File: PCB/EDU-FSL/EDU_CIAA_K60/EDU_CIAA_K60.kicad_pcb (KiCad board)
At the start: 2 copper layers, 137 x 86 mm, 188 parts, among them J1 USB OTG, J2 TB_1X2, J3 JTAG DEBUG USB, J4 JTAG DIRECTO, J5 RS485, P1 CONN_20X2, P2 CONN_20X2, Q1 2N7002, Q2 2N7002, Q3 2N7002, Q4 2N7002, Q5 2N7002, Q6 2N7002, T1 SRF2012, T2 SRF2012, U1 MIC2025-2YM, U10 MK60FX512VLQ15, U11 SI501, U2 PRTR5V0U2X, U3 NCP1117ST33T3G, U4 SI501, U5 FT2232H, U6 74HC244, U7 PRTR5V0U2X, U8 93C56, U9 SP1486EEN-L, Y1 32.768KHZ

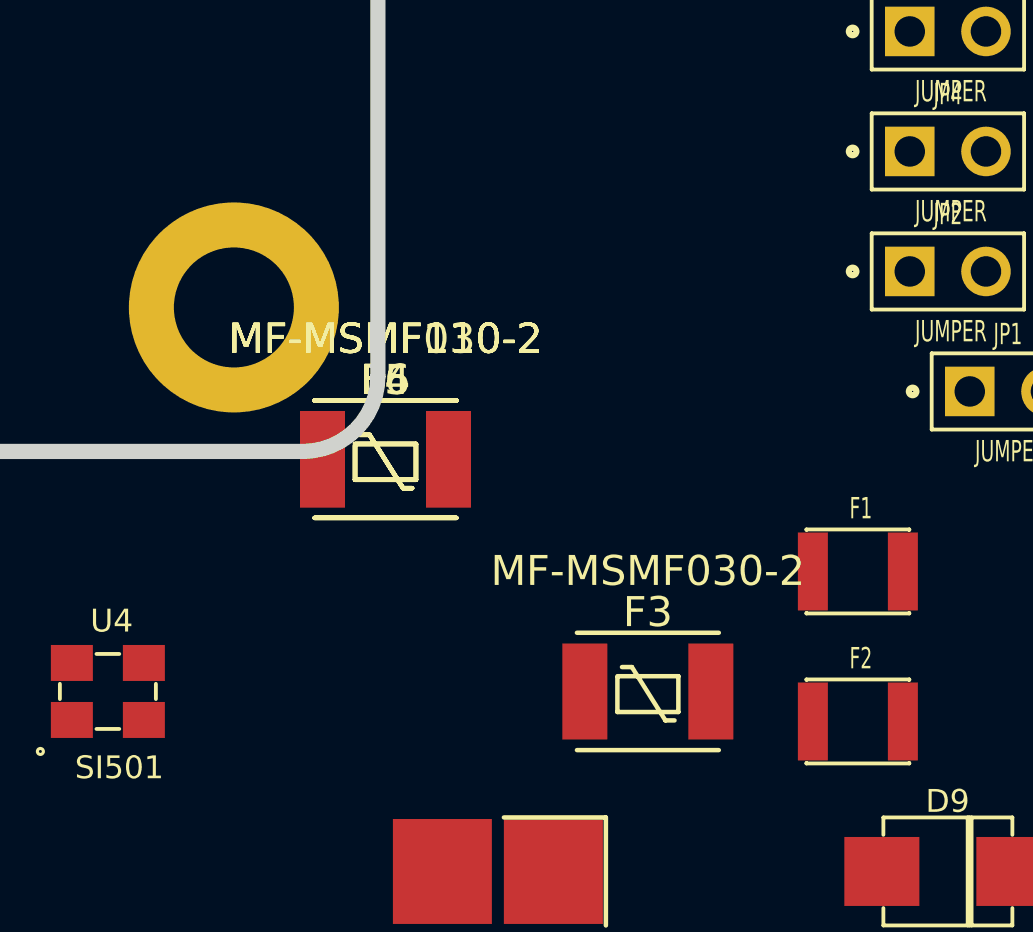
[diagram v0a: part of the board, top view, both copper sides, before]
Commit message: Modificaciones en los puertos de expansión para que sea compatible con la EDU-CIAA-NXP
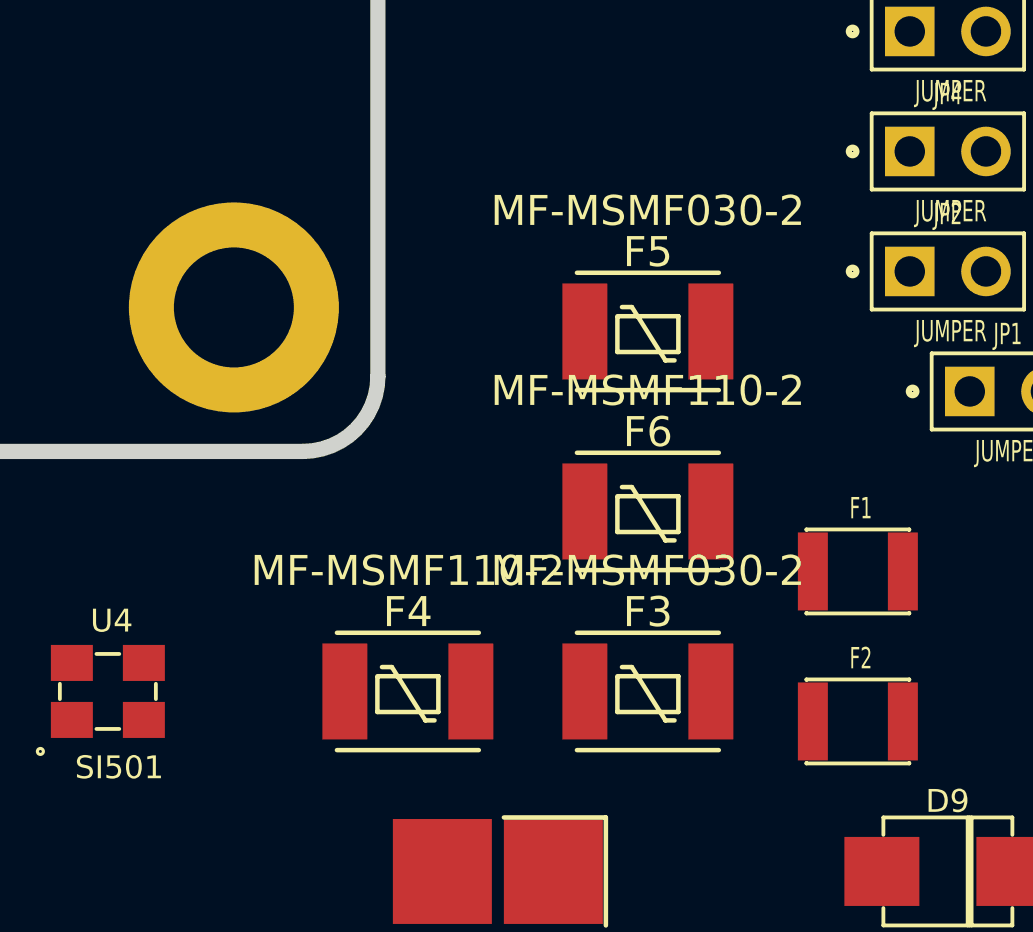
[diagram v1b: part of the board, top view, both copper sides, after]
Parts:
- moved F5 9.73 mm to (176.0, 112.0)
- moved F6 8.92 mm to (176.0, 118.0)
- moved F4 7.78 mm to (168.0, 124.0)
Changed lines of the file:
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@@
   (general
     (links 470)
-    (no_connects 469)
-    (area 29.745999 29.745999 167.254001 116.254001)
+    (no_connects 470)
+    (area 10.059402 15.34164 277.755601 166.37414)
     (thickness 1.6)
     (drawings 52)
@@
   )
   (module MF-MSMF (layer TOP)
-    (at 167.254001 116.259001)
+    (at 168 124)
     (fp_text reference F4 (at 0 -2.6416) (layer F.SilkS)
       (effects (font (size 1 1) (thickness 0.15)))
@@
   )
   (module MF-MSMF (layer TOP)
-    (at 167.254001 116.259001)
+    (at 176 118)
     (fp_text reference F6 (at 0 -2.6416) (layer F.SilkS)
       (effects (font (size 1 1) (thickness 0.15)))
@@
   )
   (module MF-MSMF (layer TOP)
-    (at 167.254001 116.259001)
+    (at 176 112)
     (fp_text reference F5 (at 0 -2.6416) (layer F.SilkS)
       (effects (font (size 1 1) (thickness 0.15)))

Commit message: Componentes ubicados en el PCB para comenzar el ruteo
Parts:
- removed R53: 22, r_0805
- added G1: LOGO, LOGO, F.Cu at (255.9, 196.9)
- J1, J3: footprint USB_MicroAB -> USB_microAB_ZX62-AB-5P8
- JP1, JP2, JP3, JP4: footprint PIN_ARRAY_2x1 -> GS2
- moved C4 209.8 mm to (301.1, 187.2)
- moved MH1 209.1 mm to (263.0, 218.8)
- moved MH3 190.0 mm to (232.3, 64.7)
- moved MH4 187.7 mm to (227.0, 69.2)
- moved FB3 177.6 mm to (266.0, 238.0)
- moved F1 177.5 mm to (329.0, 221.0)
- moved L1 176.6 mm to (246.1, 247.4)
- moved FB4 176.6 mm to (266.3, 241.1)
- moved D9 174.5 mm to (312.3, 250.4)
- moved U7 173.9 mm to (237.5, 237.7)
- moved F2 171.8 mm to (328.7, 216.0)
- moved U11 171.2 mm to (238.1, 224.2)
- moved L6 169.5 mm to (246.5, 240.8)
- moved L5 167.8 mm to (246.2, 244.6)
- moved TP1 166.8 mm to (231.1, 237.5)
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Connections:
- net /CPU/SD_DAT0 renamed /GPIO/GPIO2
- net /CPU/SD_DAT2 renamed /GPIO/GPIO4
- net /CPU/SD_POW renamed /GPIO/GPIO0
- P1 pad 11: N-00000236 -> N-00000240
- P1 pad 13: N-00000238 (its old number) -> N-00000239
- P1 pad 15: +3.3VADC -> N-00000236
- P1 pad 17: /CPU/I2C_SDA -> +3.3VADC
- P1 pad 18: GND -> GNDA
- P1 pad 19: /CPU/I2C_SCL -> /CPU/I2C_SDA
- P1 pad 21: /CPU/RS232_RXD -> /CPU/I2C_SCL
- P1 pad 22: /CPU/RS232_CTS -> GND
- P1 pad 23: /CPU/RS232_RTS -> /CPU/RS232_RXD
- P1 pad 28: /CPU/CAN_STB -> GND
- P1 pad 5: GNDA -> /CPU/ISP
- P1 pad 6: GNDA -> /CPU/WAKEUP
- P1 pad 7: N-00000240 -> GNDA
- P1 pad 9: N-00000237 -> N-00000241
- P2 pad 11: /CPU/ETH_RXER -> GND
- P2 pad 13: /CPU/ETH_RST -> GND
- P2 pad 22: /CPU/AUX_UART_RTS/SPI_CS -> /GPIO/LCD4
- P2 pad 23: GND -> /GPIO/LCD_EN
- P2 pad 24: /GPIO/LCD_EN -> /GPIO/LCD_RS
- P2 pad 26: /GPIO/LCD4 -> /GPIO/LCD3
- P2 pad 28: /GPIO/LCD_RS -> /GPIO/LCD2
- P2 pad 30: /GPIO/LCD3 -> /GPIO/LCD1
- P2 pad 32: /GPIO/LCD2 -> /GPIO/GPIO1
- P2 pad 34: /GPIO/LCD1 -> /GPIO/GPIO3
- P2 pad 35: /CPU/SD_CLK -> /GPIO/GPIO6
- P2 pad 36: /CPU/SD_CMD -> /GPIO/GPIO5
- P2 pad 38: /CPU/SD_DAT1 -> /GPIO/GPIO7
- P2 pad 40: /CPU/SD_DAT3 -> /GPIO/GPIO8
- Q1 pad D: (no net) -> N-00000233
- Q1 pad G: (no net) -> N-00000220
- Q1 pad S: (no net) -> GND
- Q2 pad D: (no net) -> N-00000223
- Q2 pad G: (no net) -> N-00000222
- Q2 pad S: (no net) -> GND
- Q3 pad D: (no net) -> N-00000217
- Q3 pad G: (no net) -> N-00000214
- Q3 pad S: (no net) -> GND
- Q4 pad D: (no net) -> N-00000224
- Q4 pad G: (no net) -> N-00000215
- Q4 pad S: (no net) -> GND
- Q5 pad D: (no net) -> N-00000231
- Q5 pad G: (no net) -> N-00000229
- Q5 pad S: (no net) -> GND
- Q6 pad D: (no net) -> N-00000221
- Q6 pad G: (no net) -> N-00000225
- Q6 pad S: (no net) -> GND
- R28 pad 2: N-00000223 -> N-00000220
- R29 pad 2: N-00000220 -> N-00000233
- R32 pad 2: N-00000225 -> N-00000222
- R34 pad 2: N-00000224 -> N-00000223
- R35 pad 2: N-00000218 (its old number) -> N-00000217
- R37 pad 2: N-00000216 (its old number) -> N-00000215
- R38 pad 2: N-00000215 -> N-00000224
- R41 pad 2: N-00000231 -> N-00000229
- R42 pad 2: N-00000227 (its old number) -> N-00000225
- R43 pad 2: N-00000233 -> N-00000231
- R44 pad 2: N-00000228 (its old number) -> N-00000221
- R45 pad 2: N-00000240 -> N-00000241
- R46 pad 2: N-00000237 -> N-00000240
- R47 pad 2: N-00000236 -> N-00000239
- R48 pad 2: N-00000238 (its old number) -> N-00000236
- U10 pad 1: /CPU/SD_DAT1 -> /GPIO/GPIO3
- U10 pad 118: (no net) -> /CPU/ISP
- U10 pad 120: (no net) -> /CPU/WAKEUP
- U10 pad 127: /CPU/AUX_UART_RTS/SPI_CS -> (no net)
- U10 pad 3: N-00000129 (its old number) -> /GPIO/GPIO6
- U10 pad 4: /CPU/SD_CMD -> /GPIO/GPIO1
- U10 pad 54: /CPU/CAN_STB -> (no net)
- U10 pad 55: /CPU/ETH_RXER -> (no net)
- U10 pad 7: /CPU/SD_DAT3 -> /GPIO/GPIO5
- U10 pad 73: /CPU/ETH_RST -> (no net)
- U10 pad 89: /CPU/RS232_RTS -> /GPIO/GPIO7
- U10 pad 90: /CPU/RS232_CTS -> /GPIO/GPIO8
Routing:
- net GND: track 0.00 -> 153.5 mm
- net +5V: track 0.00 -> 50.8 mm
- net GNDA: track 0.00 -> 26.6 mm
- net (no net): track 0.00 -> 26.0 mm
- net +3.3V: track 0.00 -> 8.24 mm
- net N-00000242: track 0.00 -> 5.31 mm
- net N-00000238: track 0.00 -> 4.93 mm
- net /JTAG/CHS_DBG: track 0.00 -> 2.50 mm
- net N-00000232: track 0.00 -> 0.60 mm
- net N-00000149: vias 0 -> 1
- removed copper zone on B.Cu, net (none)
- removed copper zone on F.Cu, net (none)
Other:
- board size 137 x 86 mm -> 85.8 x 137 mm
- net class Alimentación added: clearance 0.2032, trace_width 0.254, via_dia 0.8128, via_drill 0.4064
- net class Pistas 0.35 added: clearance 0.2032, trace_width 0.35, via_dia 0.8128, via_drill 0.4064
- net class RS485 added: clearance 0.2032, trace_width 0.254, via_dia 0.8128, via_drill 0.4064
- net class USB removed
- net class USB diff90 added: clearance 0.2032, trace_width 0.3175, via_dia 0.8128, via_drill 0.4064
- net class USB_Alimentacion added: clearance 0.2032, trace_width 0.254, via_dia 0.8128, via_drill 0.4064
- net class soporte mecanico added: clearance 0.2032, trace_width 1, via_dia 0.8128, via_drill 0.4064
- rule pad_to_mask_clearance: 0.0508 -> 0.0254
- rule via_min_drill: 0.4064 -> 0.4
- rule via_min_size: 0.8128 -> 0.8
- board text added: "+3.3V"
- board text added: "+5"
- board text added: "+5V"
- board text added: "232_RX"
- board text added: "232_TX"
- board text added: "ANALOG"
- board text added: "B"
- board text added: "CAN_RD"
- board text added: "CAN_TD"
- board text added: "CH1"
- board text added: "CH2"
- board text added: "CH3"
- board text added: "CRS_DV"
- board text added: "DAC"
- board text added: "DEBUG"
- board text added: "EDU-CIAA-FSL"
- board text added: "ETHERNET"
- board text added: "G"
- board text added: "GND"
- board text added: "GNDA"
- board text added: "GPIO0"
- board text added: "GPIO1"
- board text added: "GPIO2"
- board text added: "GPIO3"
- board text added: "GPIO4"
- board text added: "GPIO5"
- board text added: "GPIO6"
- board text added: "GPIO7"
- board text added: "GPIO8"
- board text added: "I2C_SCL"
- board text added: "I2C_SDA"
- board text added: "ISP"
- board text added: "J4"
- board text added: "LCD1"
- board text added: "LCD2"
- board text added: "LCD3"
- board text added: "LCD4"
- board text added: "LCD_EN"
- board text added: "LCD_RS"
- board text added: "LED 1"
- board text added: "LED 2"
- board text added: "LED 3"
- board text added: "MDC"
- board text added: "MDIO"
- board text added: "P1"
- board text added: "P2"
- board text added: "R"
- board text added: "REF_CLK"
- board text added: "RESET"
- board text added: "RS485"
- board text added: "RXD0"
- board text added: "RXD1"
- board text added: "SPI_MISO"
- board text added: "SPI_MOSI"
- board text added: "SPI_SCK"
- board text added: "TEC 1"
- board text added: "TEC 2"
- board text added: "TEC 3"
- board text added: "TEC 4"
- board text added: "TXD0"
- board text added: "TXD1"
- board text added: "TX_EN"
- board text added: "T_C2"
- board text added: "T_COL0"
- board text added: "T_COL1"
- board text added: "T_F1"
- board text added: "T_FIL0"
- board text added: "T_FIL2"
- board text added: "T_FIL3"
- board text added: "USB OTG"
- board text added: "V0.0"
- board text added: "VDDA"
- board text added: "WAKEUP"
- board text removed: "Verificador de espesores"

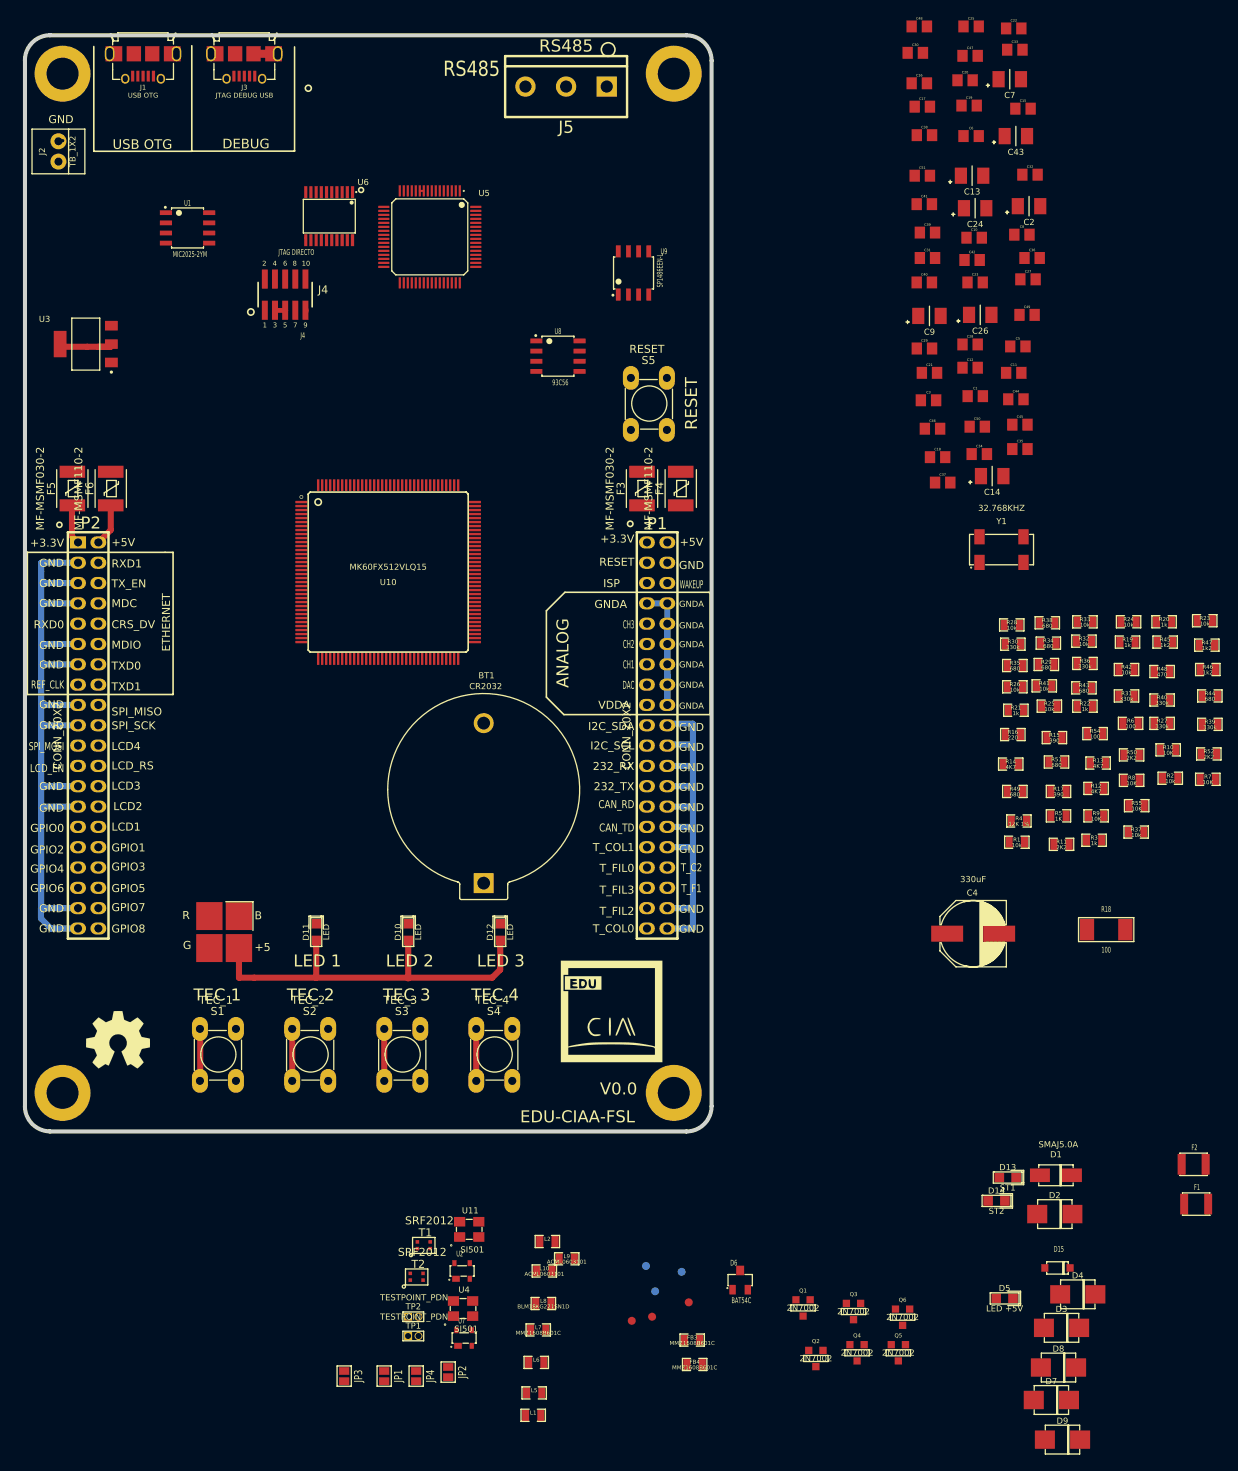
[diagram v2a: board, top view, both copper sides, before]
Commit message: Componentes reordenados en el PCB listo para rutear
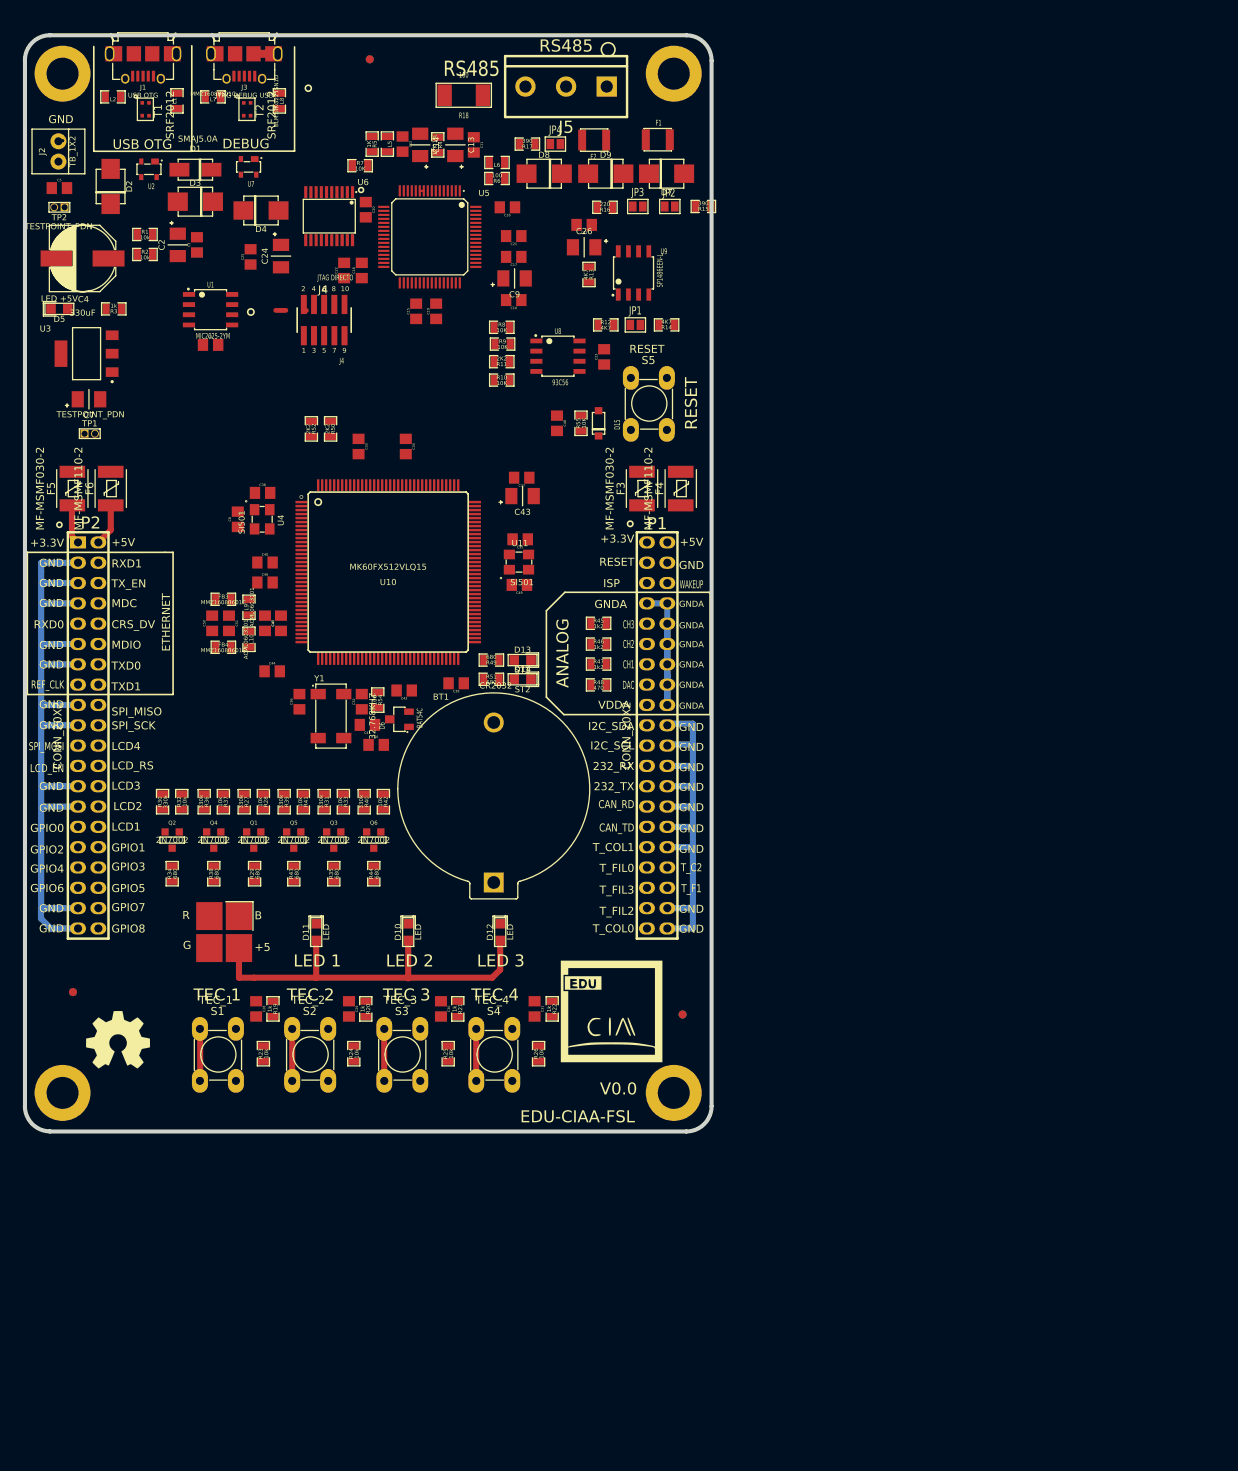
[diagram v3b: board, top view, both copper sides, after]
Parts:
- moved D3 177.6 mm to (203.9, 95.7)
- moved D2 174.4 mm to (193.3, 93.8), turned to 270 degrees
- moved D5 171.1 mm to (186.9, 109.1), turned to 180 degrees
- moved L1 170.2 mm to (201.6, 83.1), turned to 90 degrees
- moved D4 169.6 mm to (212.1, 96.8), turned to 180 degrees
- moved D9 168.2 mm to (255.2, 92.2)
- moved D1 165.4 mm to (203.9, 91.7)
- moved D8 162.5 mm to (247.5, 92.2)
- moved FD4 161.1 mm to (225.7, 77.9)
- moved D7 160.7 mm to (262.8, 92.2), turned to 180 degrees
- moved L7 159.4 mm to (206.1, 82.6), turned to 180 degrees
- moved FD5 158.1 mm to (225.7, 77.9)
- moved L5 157.2 mm to (227.9, 88.5), turned to 270 degrees
- moved JP4 155.0 mm to (248.9, 88.5), turned to 90 degrees
- moved L8 153.9 mm to (214.4, 83.1), turned to 270 degrees
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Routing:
- net +3.3V: track 8.24 -> 0.00 mm
- net GND: track 153.5 -> 152.2 mm
- net (no net): track 26.0 -> 27.3 mm
